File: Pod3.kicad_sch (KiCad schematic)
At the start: 156 parts, among them U71 1NB4-5036 Comparator, U72 1NB4-5036 Comparator

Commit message: Add component values, some more nets
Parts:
- C253, C264, C265, C267, C269, C271, C273, C274, C275, C277, C278, C298, C299, C300, C301, C302, C304, C307, C308, C309, C310, C311, C312: value 330pF -> 360pF
- C272, C276: value ? -> 0.047uF
- C306: value ? -> 1nF
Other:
- note removed: "U21 pin K26"
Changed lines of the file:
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@@
 	(generator_version "9.0")
 	(paper "A2")
-	(text "U21 pin K26"
-		(exclude_from_sim no)
-		(at 548.132 54.356 0)
-		(effects
-			(font
-				(size 1.27 1.27)
-			)
-		)
-	)
 	(text "POD 3"
 		(exclude_from_sim no)
@@
 	(wire
 		(pts
-			(xy 476.25 172.72) (xy 476.25 179.07)
-		)
-		(stroke
-			(width 0)
-			(type default)
-		)
-	)
-	(wire
-		(pts
 			(xy 502.92 149.86) (xy 506.73 149.86)
 		)
@@
 	(wire
 		(pts
-			(xy 472.44 176.53) (xy 472.44 172.72)
-		)
-		(stroke
-			(width 0)
-			(type default)
-		)
-	)
-	(wire
-		(pts
 			(xy 546.1 170.18) (xy 528.32 170.18)
 		)
@@
 	(wire
 		(pts
-			(xy 472.44 172.72) (xy 476.25 172.72)
-		)
-		(stroke
-			(width 0)
-			(type default)
-		)
-	)
-	(wire
-		(pts
 			(xy 499.11 86.36) (xy 486.41 86.36)
 		)
@@
 	(wire
 		(pts
-			(xy 476.25 184.15) (xy 476.25 186.69)
-		)
-		(stroke
-			(width 0)
-			(type default)
-		)
-	)
-	(wire
-		(pts
 			(xy 172.72 52.07) (xy 172.72 53.34)
 		)
@@
 			)
 		)
-		(property "Value" "330pF"
+		(property "Value" "360pF"
 			(at 138.43 123.1962 0)
 			(effects
@@
 			)
 		)
-		(property "Value" "330pF"
+		(property "Value" "360pF"
 			(at 458.47 153.6762 0)
 			(effects
@@
 			)
 		)
-		(property "Value" "330pF"
+		(property "Value" "360pF"
 			(at 470.154 153.924 0)
 			(effects
@@
 			)
 		)
-		(property "Value" "330pF"
+		(property "Value" "360pF"
 			(at 217.17 41.9162 0)
 			(effects
@@
 			)
 		)
-		(property "Value" "330pF"
+		(property "Value" "360pF"
 			(at 453.39 46.9962 0)
 			(effects
@@
 			)
 		)
-		(property "Value" "330pF"
+		(property "Value" "360pF"
 			(at 491.49 46.9962 0)
 			(effects
@@
 			)
 		)
-		(property "Value" "330pF"
+		(property "Value" "360pF"
 			(at 201.93 41.9162 0)
 			(effects
@@
 			)
 		)
-		(property "Value" "330pF"
+		(property "Value" "360pF"
 			(at 411.48 138.4362 0)
 			(effects
@@
 	(symbol
 		(lib_id "power:GND")
-		(at 472.44 176.53 0)
-		(mirror y)
-		(unit 1)
-		(exclude_from_sim no)
-		(in_bom yes)
-		(on_board yes)
-		(dnp no)
-		(fields_autoplaced yes)
-		(property "Reference" "#PWR0550"
-			(at 472.44 182.88 0)
-			(effects
-				(font
-					(size 1.27 1.27)
-				)
-				(hide yes)
-			)
-		)
-		(property "Value" "GND"
-			(at 472.44 181.61 0)
-			(effects
-				(font
-					(size 1.27 1.27)
-				)
-				(hide yes)
-			)
-		)
-		(property "Footprint" ""
-			(at 472.44 176.53 0)
-			(effects
-				(font
-					(size 1.27 1.27)
-				)
-				(hide yes)
-			)
-		)
-		(property "Datasheet" ""
-			(at 472.44 176.53 0)
-			(effects
-				(font
-					(size 1.27 1.27)
-				)
-				(hide yes)
-			)
-		)
-		(property "Description" "Power symbol creates a global label with name \"GND\" , ground"
-			(at 472.44 176.53 0)
-			(effects
-				(font
-					(size 1.27 1.27)
-				)
-				(hide yes)
-			)
-		)
-		(pin "1"
-		)
-		(instances
-			(project "hp16717"
-				(path "/173036db-20dd-4729-b214-c668df2e6caa/0626cbb8-19d6-4076-966a-8b99b5ddee68"
-					(reference "#PWR0550")
-					(unit 1)
-				)
-			)
-		)
-	)
-	(symbol
-		(lib_id "power:GND")
 		(at 73.66 186.69 0)
 		(unit 1)
@@
 			)
 		)
-		(property "Value" "330pF"
+		(property "Value" "360pF"
 			(at 153.67 41.9162 0)
 			(effects
@@
 			)
 		)
-		(property "Value" "330pF"
+		(property "Value" "360pF"
 			(at 163.83 41.9162 0)
 			(effects
@@
 			)
 		)
-		(property "Value" "?"
+		(property "Value" "0.047uF"
 			(at 207.264 162.814 0)
 			(effects
@@
 			)
 		)
-		(property "Value" "?"
+		(property "Value" "0.047uF"
 			(at 197.104 162.814 0)
 			(effects
@@
 			)
 		)
-		(property "Value" "330pF"
+		(property "Value" "360pF"
 			(at 72.3963 252.73 90)
 			(effects
@@
 			)
 		)
-		(property "Value" "330pF"
+		(property "Value" "360pF"
 			(at 499.11 46.9962 0)
 			(effects
@@
 			)
 		)
-		(property "Value" "330pF"
+		(property "Value" "360pF"
 			(at 448.31 153.6762 0)
 			(effects
@@
 			)
 		)
-		(property "Value" "330pF"
+		(property "Value" "360pF"
 			(at 194.564 138.684 0)
 			(effects
@@
 			)
 		)
-		(property "Value" "330pF"
+		(property "Value" "360pF"
 			(at 204.216 138.176 0)
 			(effects
@@
 			)
 		)
-		(property "Value" "330pF"
+		(property "Value" "360pF"
 			(at 182.88 138.4362 0)
 			(effects
@@
 			)
 		)
-		(property "Value" "?"
+		(property "Value" "1nF"
 			(at 507.746 47.244 0)
 			(effects
@@
 			)
 		)
-		(property "Value" "330pF"
+		(property "Value" "360pF"
 			(at 172.72 138.4362 0)
 			(effects
@@
 	)
 	(symbol
-		(lib_id "power:-5V")
-		(at 476.25 186.69 180)
-		(unit 1)
-		(exclude_from_sim no)
-		(in_bom yes)
-		(on_board yes)
-		(dnp no)
-		(fields_autoplaced yes)
-		(property "Reference" "#PWR0551"
-			(at 476.25 182.88 0)
-			(effects
-				(font
-					(size 1.27 1.27)
-				)
-				(hide yes)
-			)
-		)
-		(property "Value" "-5V2"
-			(at 476.25 191.77 0)
-			(effects
-				(font
-					(size 1.27 1.27)
-				)
-			)
-		)
-		(property "Footprint" ""
-			(at 476.25 186.69 0)
-			(effects
-				(font
-					(size 1.27 1.27)
-				)
-				(hide yes)
-			)
-		)
-		(property "Datasheet" ""
-			(at 476.25 186.69 0)
-			(effects
-				(font
-					(size 1.27 1.27)
-				)
-				(hide yes)
-			)
-		)
-		(property "Description" "Power symbol creates a global label with name \"-5V\""
-			(at 476.25 186.69 0)
-			(effects
-				(font
-					(size 1.27 1.27)
-				)
-				(hide yes)
-			)
-		)
-		(pin "1"
-		)
-		(instances
-			(project "hp16717"
-				(path "/173036db-20dd-4729-b214-c668df2e6caa/0626cbb8-19d6-4076-966a-8b99b5ddee68"
-					(reference "#PWR0551")
-					(unit 1)
-				)
-			)
-		)
-	)
-	(symbol
 		(lib_id "Device:C_Small")
 		(at 69.85 190.5 90)
@@
 			)
 		)
-		(property "Value" "330pF"
+		(property "Value" "360pF"
 			(at 483.87 46.9962 0)
 			(effects
@@
 			)
 		)
-		(property "Value" "330pF"
+		(property "Value" "360pF"
 			(at 479.806 153.416 0)
 			(effects
@@
 			)
 		)
-		(property "Value" "330pF"
+		(property "Value" "360pF"
 			(at 209.55 41.9162 0)
 			(effects
@@
 			)
 		)
-		(property "Value" "330pF"
+		(property "Value" "360pF"
 			(at 194.31 41.9162 0)
 			(effects
@@
 			)
 		)
-		(property "Value" "330pF"
+		(property "Value" "360pF"
 			(at 476.25 46.9962 0)
 			(effects
@@
 			)
 		)
-		(property "Value" "330pF"
+		(property "Value" "360pF"
 			(at 444.5 46.9962 0)
 			(effects

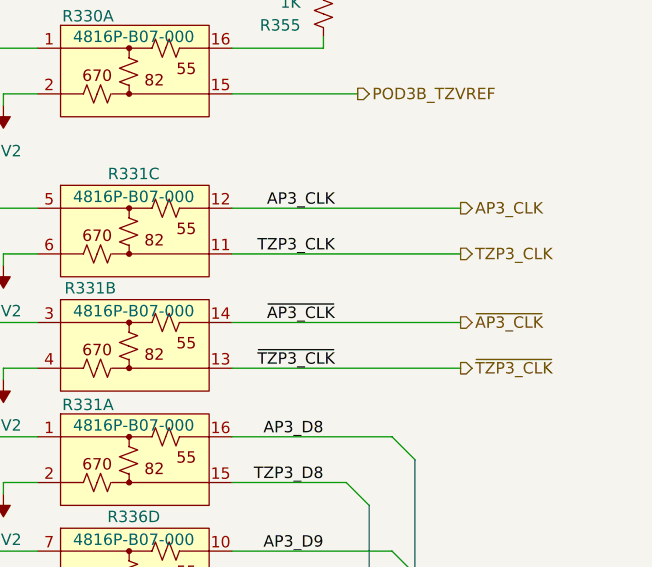
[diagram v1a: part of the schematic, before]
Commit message: complete outer layers
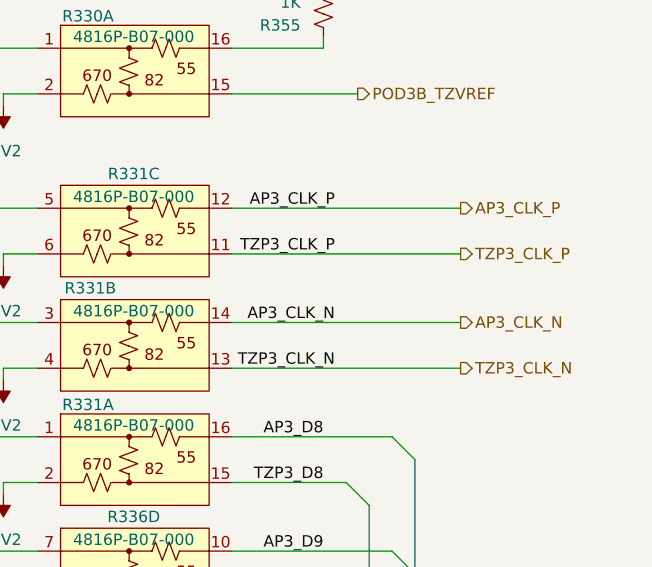
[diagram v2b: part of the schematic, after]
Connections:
- net AP3_CLK renamed AP3_CLK_P
- net TZP3_CLK renamed TZP3_CLK_P
- net ~{AP3_CLK} renamed AP3_CLK_N
- net ~{TZP3_CLK} renamed TZP3_CLK_N
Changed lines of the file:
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@@
 		)
 	)
-	(label "~{AP3_CLK}"
+	(label "AP3_CLK_N"
 		(at 539.75 93.98 180)
 		(effects
@@
 		)
 	)
-	(label "AP3_CLK"
+	(label "AP3_CLK_P"
 		(at 539.75 81.28 180)
 		(effects
@@
 		)
 	)
-	(label "~{TZP3_CLK}"
+	(label "TZP3_CLK_N"
 		(at 539.75 99.06 180)
 		(effects
@@
 		)
 	)
-	(label "TZP3_CLK"
+	(label "TZP3_CLK_P"
 		(at 539.75 86.36 180)
 		(effects
@@
 		)
 	)
-	(hierarchical_label "~{AP3_CLK}"
+	(hierarchical_label "AP3_CLK_N"
 		(shape output)
 		(at 553.72 93.98 0)
@@
 		)
 	)
-	(hierarchical_label "AP3_CLK"
+	(hierarchical_label "AP3_CLK_P"
 		(shape output)
 		(at 553.72 81.28 0)
@@
 		)
 	)
-	(hierarchical_label "~{TZP3_CLK}"
+	(hierarchical_label "TZP3_CLK_N"
 		(shape output)
 		(at 553.72 99.06 0)
@@
 		)
 	)
-	(hierarchical_label "TZP3_CLK"
+	(hierarchical_label "TZP3_CLK_P"
 		(shape output)
 		(at 553.72 86.36 0)

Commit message: add test points
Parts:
- added TP1020, TP1021, TP1047: ?, hp16717:HP_TP30, symbol Connector:TestPoint_Alt
- added TP1025, TP1041: +3V3, hp16717:HP_TP30, symbol Connector:TestPoint_Alt
- added TP1026, TP1032, TP1034, TP1040, TP1049, TP1054, TP1055: GND, hp16717:HP_TP30, symbol Connector:TestPoint_Alt
- added TP1027, TP1035: CMP9, hp16717:HP_TP30, symbol Connector:TestPoint_Alt
- added TP1028, TP1036: CMP8, hp16717:HP_TP30, symbol Connector:TestPoint_Alt
- added TP1029: CMP1_P, hp16717:HP_TP30, symbol Connector:TestPoint_Alt
- added TP1030: CMP1_N, hp16717:HP_TP30, symbol Connector:TestPoint_Alt
- added TP1033: CMP6, hp16717:HP_TP30, symbol Connector:TestPoint_Alt
- added TP1037: CMP7, hp16717:HP_TP30, symbol Connector:TestPoint_Alt
- added TP1038: CMP3, hp16717:HP_TP30, symbol Connector:TestPoint_Alt
- added TP1039: CMP2, hp16717:HP_TP30, symbol Connector:TestPoint_Alt
- added TP1042: -3V3, hp16717:HP_TP30, symbol Connector:TestPoint_Alt
- added TP1045, TP1048: -5V2, hp16717:HP_TP30, symbol Connector:TestPoint_Alt
- added TP1056: PO3_4_TEST, hp16717:HP_TP30, symbol Connector:TestPoint_Alt
- added TP979: POD3A_VREF, hp16717:HP_TP30, symbol Connector:TestPoint_Alt
- added TP980: POD3B_VREF, hp16717:HP_TP30, symbol Connector:TestPoint_Alt
- added TP987: POD3B_TZVREF, hp16717:HP_TP30, symbol Connector:TestPoint_Alt
- added TP988: POD3A_TZVREF, hp16717:HP_TP30, symbol Connector:TestPoint_Alt
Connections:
- net +3V3: now also TP1025.1, TP1041.1
- net -3V3: now also TP1042.1
- net -5V2: now also TP1045.1, TP1048.1
- net GND: now also TP1026.1, TP1032.1, TP1034.1, TP1040.1, TP1049.1, TP1054.1, TP1055.1
- net POD3A_TZVREF: now also TP988.1
- net POD3A_VREF: now also TP979.1
- net POD3B_TZVREF: now also TP987.1
- net POD3B_VREF: now also TP980.1
- net POD3_4_TEST_SIG: now also TP1056.1
- net at R331.3, U71.8 (CMP_OUT1): now also TP1029.1
- net at R311.1, R337.10: now also TP1047.1
- net at R330.16, R355.1: now also TP1020.1
- net at R338.5, U72.12 (CMP_OUT3): now also TP1038.1
- net at R330.5, U71.25 (CMP_OUT8): now also TP1028.1
- net at R336.1, U71.21 (CMP_OUT6): now also TP1033.1
- net at R337.1, U72.25 (CMP_OUT8): now also TP1036.1
- net at R330.1, U71.19 (2V1?): now also TP1021.1
- net at R338.7, U72.10 (CMP_OUT2): now also TP1039.1
- net at R337.3, U72.23 (CMP_OUT7): now also TP1037.1
- net at R331.7, U72.27 (CMP_OUT9): now also TP1035.1
- net at R330.3, U71.27 (CMP_OUT9): now also TP1027.1
- net at R331.5, U71.7 (CMP_OUT1): now also TP1030.1
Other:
- moved on the sheet: C272, C276
